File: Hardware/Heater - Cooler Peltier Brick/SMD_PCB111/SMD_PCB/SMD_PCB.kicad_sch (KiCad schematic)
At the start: 57 parts, among them J1 +12V_IN, J2 GND_IN, J3 Conn_01x06_Pin, J4 Conn_01x10_Pin, J5 Pelt1+, J7 Pelt1-, J8 Pelt2+, J9 Pelt2-, Q1 IRF3205, Q2 IRF3205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

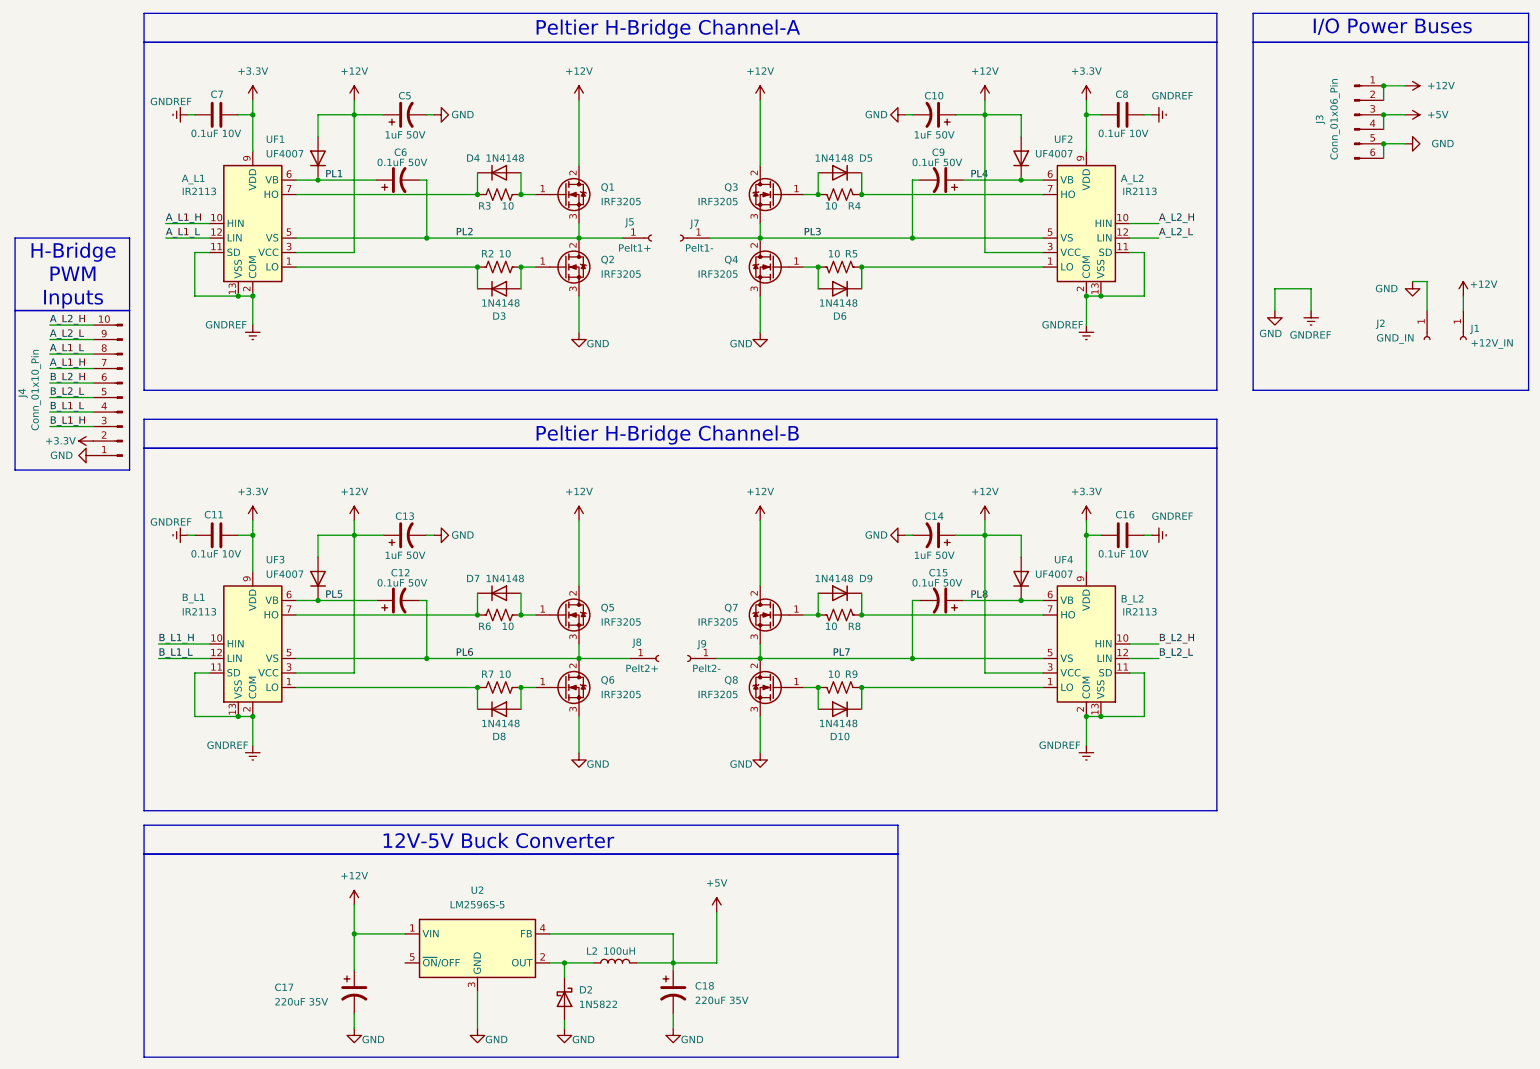
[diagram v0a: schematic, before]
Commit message: Add GUI module, update PCB design, and improve README documentation
Signed-off-by: JiaHe_Xu <jiahexu@arizona.edu>
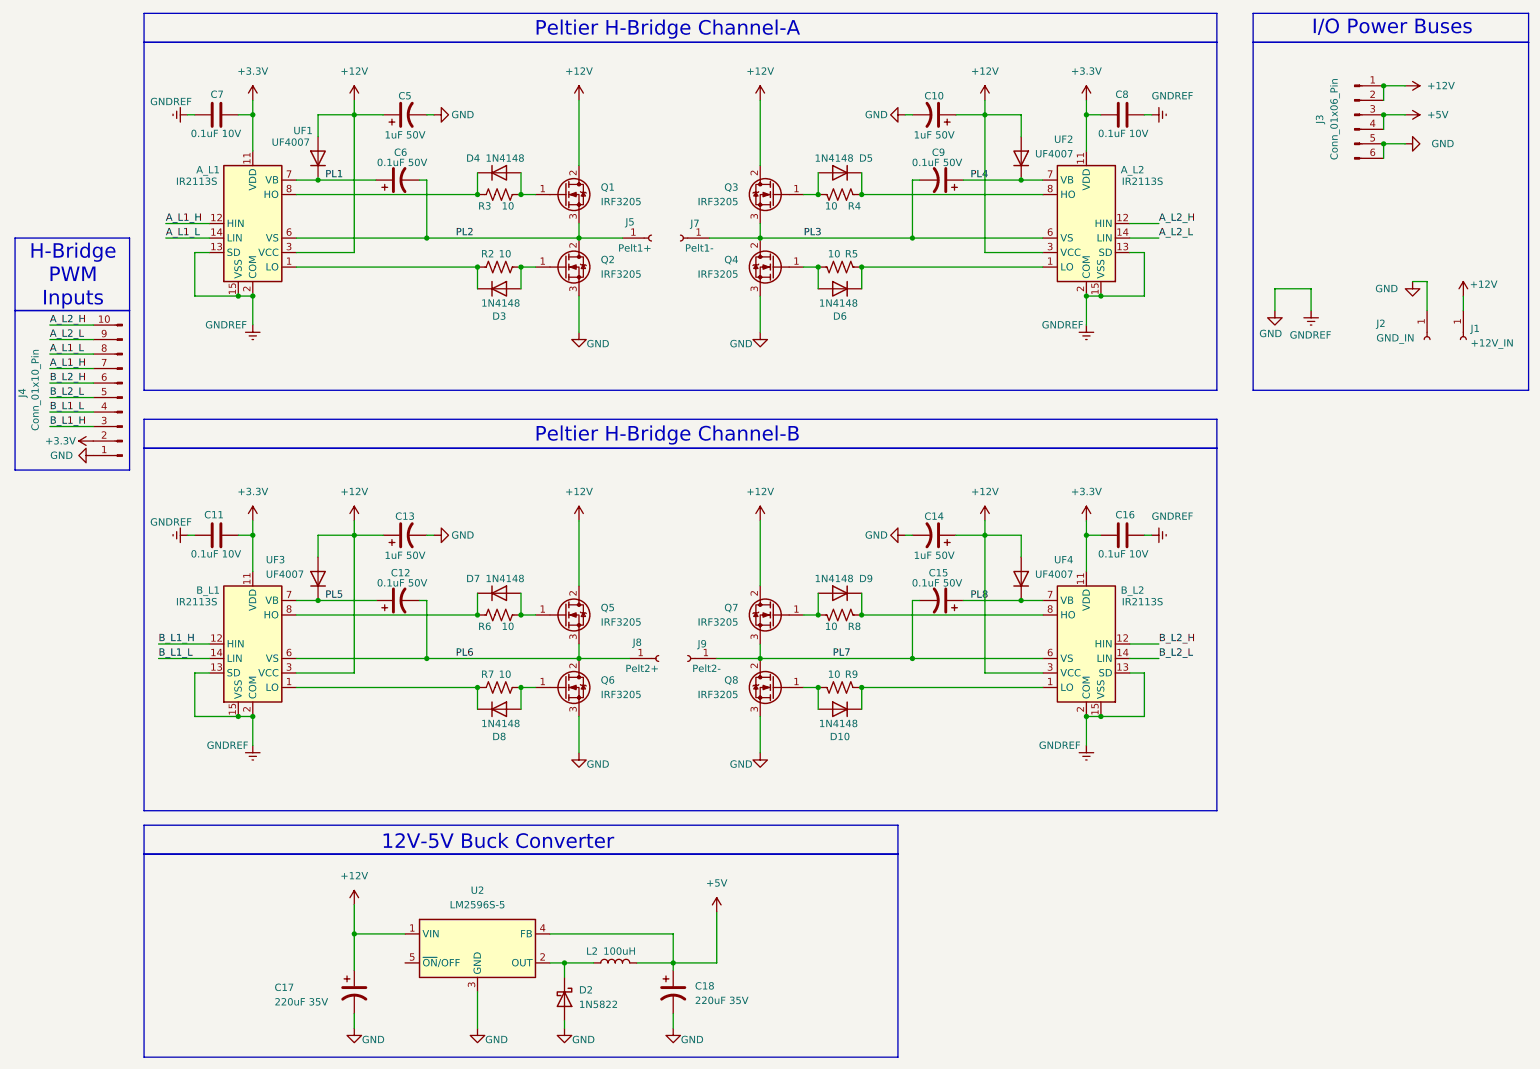
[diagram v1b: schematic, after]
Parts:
- removed A_L1, A_L2, B_L1, B_L2: IR2113, Package_SO:SOIC-16W_7.5x10.3mm_P1.27mm, symbol Driver_FET:IR2113
- added A_L1, A_L2, B_L1, B_L2: IR2113S, Package_SO:SOIC-16W_7.5x10.3mm_P1.27mm, symbol Driver_FET:IR2113S
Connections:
- net +12V: now also A_L1.3 (VCC), A_L2.3 (VCC), B_L1.3 (VCC), B_L2.3 (VCC)
- net +3.3V: now also A_L1.11 (VDD), A_L2.11 (VDD), B_L1.11 (VDD), B_L2.11 (VDD)
- net A_L1_H: now also A_L1.12 (HIN)
- net A_L1_L: now also A_L1.14 (LIN)
- net A_L2_H: now also A_L2.12 (HIN)
- net A_L2_L: now also A_L2.14 (LIN)
- net B_L1_H: now also B_L1.12 (HIN)
- net B_L1_L: now also B_L1.14 (LIN)
- net B_L2_H: now also B_L2.12 (HIN)
- net B_L2_L: now also B_L2.14 (LIN)
- net GND: now also A_L1.13 (SD), A_L1.15 (VSS), A_L1.2 (COM), A_L2.13 (SD), A_L2.15 (VSS), A_L2.2 (COM), B_L1.13 (SD), B_L1.15 (VSS), B_L1.2 (COM), B_L2.13 (SD), B_L2.15 (VSS), B_L2.2 (COM)
- net PL1: now also A_L1.7 (VB)
- net PL2: now also A_L1.6 (VS)
- net PL3: now also A_L2.6 (VS)
- net PL4: now also A_L2.7 (VB)
- net PL5: now also B_L1.7 (VB)
- net PL6: now also B_L1.6 (VS)
- net PL7: now also B_L2.6 (VS)
- net PL8: now also B_L2.7 (VB)
- net at D4.1 (K), R3.1: now also A_L1.8 (HO)
- net at D3.1 (K), R2.1: now also A_L1.1 (LO)
- net at D9.1 (K), R8.1: now also B_L2.8 (HO)
- net at D6.1 (K), R5.1: now also A_L2.1 (LO)
- net at D10.1 (K), R9.1: now also B_L2.1 (LO)
- net at D7.1 (K), R6.1: now also B_L1.8 (HO)
- net at D5.1 (K), R4.1: now also A_L2.8 (HO)
- net at D8.1 (K), R7.1: now also B_L1.1 (LO)
